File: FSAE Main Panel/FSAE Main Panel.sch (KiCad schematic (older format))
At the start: 11 parts, among them U1 SAMD21G18A-AU, Y101 32.768kHz

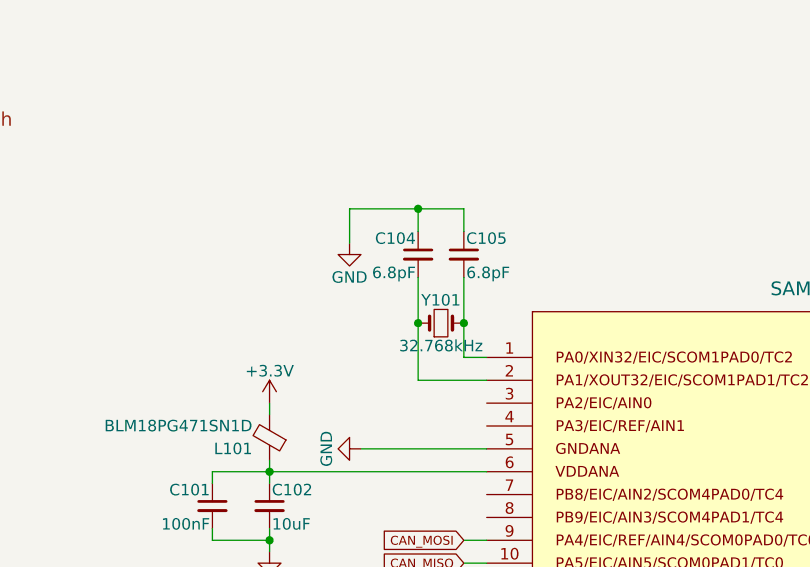
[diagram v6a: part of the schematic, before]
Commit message: Updated Footprint Association
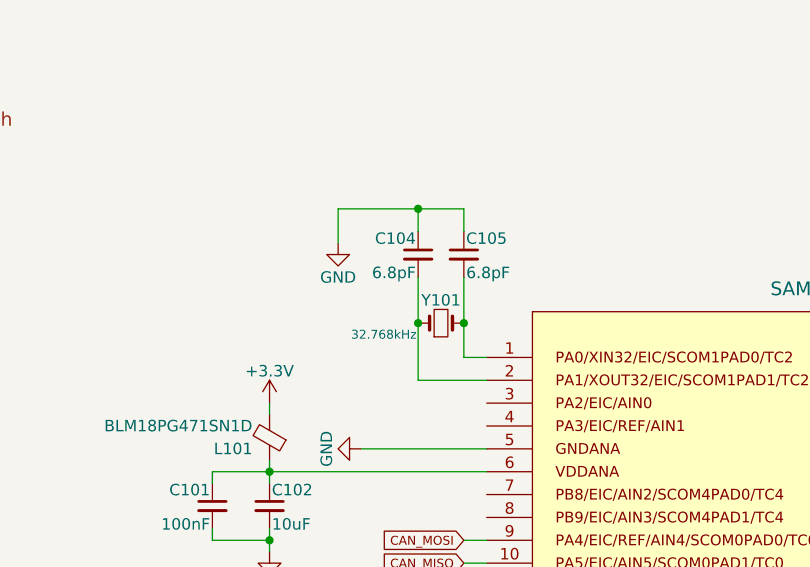
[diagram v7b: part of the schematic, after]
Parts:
- C101, C103, C106, C107: footprint (none) -> Capacitors_SMD:C_1206; Description (none) -> Ceramic 0.1uF 10V X7R 1206
- C102: footprint (none) -> Capacitors_SMD:C_1206; Description (none) -> Ceramic 10uF 25V X5R 1206
- C104, C105: footprint (none) -> Capacitors_SMD:C_0805; Description (none) -> Ceramic 6.8pF 50V C0G/NP0 0805
- C108: footprint (none) -> Capacitors_SMD:C_1206; Description (none) -> Ceramic 0.1uF 10V X7R
- L101: footprint (none) -> Inductors_SMD:L_1806
- U1: footprint (none) -> Housings_QFP:TQFP-48_7x7mm_Pitch0.5mm
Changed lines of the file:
@@
 F 0 "U1" H 5450 1800 60  0000 C CNN
 F 1 "SAMD21G18A-AU" H 5450 5000 60  0000 C CNN
-F 2 "" H 2350 3000 60  0001 C CNN
+F 2 "Housings_QFP:TQFP-48_7x7mm_Pitch0.5mm" H 2350 3000 60  0001 C CNN
 F 3 "" H 2350 3000 60  0001 C CNN
 	1    5450 3400
@@
 $EndComp
 $Comp
-L power:GND #PWR104
+L power:GND #PWR0104
 U 1 1 5BC6953B
-P 3250 1600
-F 0 "#PWR104" H 3250 1350 50  0001 C CNN
-F 1 "GND" H 3250 1450 50  0000 C CNN
-F 2 "" H 3250 1600 50  0001 C CNN
-F 3 "" H 3250 1600 50  0001 C CNN
-	1    3250 1600
-	1    0    0    -1
-$EndComp
-$Comp
-L power:+3V3 #PWR105
+P 3200 1600
+F 0 "#PWR0104" H 3200 1350 50  0001 C CNN
+F 1 "GND" H 3200 1450 50  0000 C CNN
+F 2 "" H 3200 1600 50  0001 C CNN
+F 3 "" H 3200 1600 50  0001 C CNN
+	1    3200 1600
+	1    0    0    -1
+$EndComp
+$Comp
+L power:+3V3 #PWR0105
 U 1 1 5BCFEE2B
 P 3250 3900
-F 0 "#PWR105" H 3250 3750 50  0001 C CNN
+F 0 "#PWR0105" H 3250 3750 50  0001 C CNN
 F 1 "+3V3" H 3250 4040 50  0000 C CNN
 F 2 "" H 3250 3900 50  0001 C CNN
@@
 $EndComp
 $Comp
-L power:+3V3 #PWR109
+L power:+3V3 #PWR0109
 U 1 1 5BCFEE84
 P 7150 3500
-F 0 "#PWR109" H 7150 3350 50  0001 C CNN
+F 0 "#PWR0109" H 7150 3350 50  0001 C CNN
 F 1 "+3V3" H 7150 3640 50  0000 C CNN
 F 2 "" H 7150 3500 50  0001 C CNN
@@
 $EndComp
 $Comp
-L power:+3V3 #PWR112
+L power:+3V3 #PWR0112
 U 1 1 5BCFEEDD
 P 7750 2400
-F 0 "#PWR112" H 7750 2250 50  0001 C CNN
+F 0 "#PWR0112" H 7750 2250 50  0001 C CNN
 F 1 "+3V3" H 7750 2540 50  0000 C CNN
 F 2 "" H 7750 2400 50  0001 C CNN
@@
 $EndComp
 $Comp
-L power:GND #PWR110
+L power:GND #PWR0110
 U 1 1 5BCFF22A
 P 7350 3700
-F 0 "#PWR110" H 7350 3450 50  0001 C CNN
+F 0 "#PWR0110" H 7350 3450 50  0001 C CNN
 F 1 "GND" H 7350 3550 50  0000 C CNN
 F 2 "" H 7350 3700 50  0001 C CNN
@@
 $EndComp
 $Comp
-L power:GND #PWR107
+L power:GND #PWR0107
 U 1 1 5BCFF970
 P 3300 4100
-F 0 "#PWR107" H 3300 3850 50  0001 C CNN
+F 0 "#PWR0107" H 3300 3850 50  0001 C CNN
 F 1 "GND" H 3300 3950 50  0000 C CNN
 F 2 "" H 3300 4100 50  0001 C CNN
@@
 $EndComp
 $Comp
-L power:GND #PWR108
+L power:GND #PWR0108
 U 1 1 5BCFFACD
 P 7150 2700
-F 0 "#PWR108" H 7150 2450 50  0001 C CNN
+F 0 "#PWR0108" H 7150 2450 50  0001 C CNN
 F 1 "GND" H 7150 2550 50  0000 C CNN
 F 2 "" H 7150 2700 50  0001 C CNN
@@
 $EndComp
 $Comp
-L power:GND #PWR101
+L power:GND #PWR0101
 U 1 1 5BD00189
 P 2800 4000
-F 0 "#PWR101" H 2800 3750 50  0001 C CNN
+F 0 "#PWR0101" H 2800 3750 50  0001 C CNN
 F 1 "GND" H 2800 3850 50  0000 C CNN
 F 2 "" H 2800 4000 50  0001 C CNN
@@
 $EndComp
 $Comp
-L power:GND #PWR113
+L power:GND #PWR0113
 U 1 1 5BD001EE
 P 8400 2600
-F 0 "#PWR113" H 8400 2350 50  0001 C CNN
+F 0 "#PWR0113" H 8400 2350 50  0001 C CNN
 F 1 "GND" H 8400 2450 50  0000 C CNN
 F 2 "" H 8400 2600 50  0001 C CNN
@@
 $EndComp
 $Comp
-L power:GND #PWR111
+L power:GND #PWR0111
 U 1 1 5BD006AA
 P 7550 3600
-F 0 "#PWR111" H 7550 3350 50  0001 C CNN
+F 0 "#PWR0111" H 7550 3350 50  0001 C CNN
 F 1 "GND" H 7550 3450 50  0000 C CNN
 F 2 "" H 7550 3600 50  0001 C CNN
@@
 Pins that support I2C: PA8, PA9, PA12, PA13, PA16, PA17, PA22, PA23
 $Comp
-L power:+3.3V #PWR102
+L power:+3.3V #PWR0102
 U 1 1 5BF9A879
 P 2900 2300
-F 0 "#PWR102" H 2900 2150 50  0001 C CNN
+F 0 "#PWR0102" H 2900 2150 50  0001 C CNN
 F 1 "+3.3V" H 2900 2440 50  0000 C CNN
 F 2 "" H 2900 2300 50  0001 C CNN
@@
 $EndComp
 $Comp
-L power:GND #PWR106
+L power:GND #PWR0106
 U 1 1 5BF9A928
 P 3300 2500
-F 0 "#PWR106" H 3300 2250 50  0001 C CNN
+F 0 "#PWR0106" H 3300 2250 50  0001 C CNN
 F 1 "GND" H 3300 2350 50  0000 C CNN
 F 2 "" H 3300 2500 50  0001 C CNN
@@
 $EndComp
 $Comp
-L power:GND #PWR103
+L power:GND #PWR0103
 U 1 1 5BF9AD79
 P 2900 2950
-F 0 "#PWR103" H 2900 2700 50  0001 C CNN
+F 0 "#PWR0103" H 2900 2700 50  0001 C CNN
 F 1 "GND" H 2900 2800 50  0000 C CNN
 F 2 "" H 2900 2950 50  0001 C CNN
@@
 F 0 "L101" H 2975 2500 50  0000 L CNN
 F 1 "BLM18PG471SN1D" H 2975 2400 50  0000 L CNN
-F 2 "" V 2830 2450 50  0001 C CNN
+F 2 "Inductors_SMD:L_1806" V 2830 2450 50  0001 C CNN
 F 3 "" H 2900 2450 50  0001 C CNN
 	1    2900 2450
@@
 F 0 "C102" H 2910 2820 50  0000 L CNN
 F 1 "10uF" H 2910 2670 50  0000 L CNN
-F 2 "" H 2900 2750 50  0001 C CNN
+F 2 "Capacitors_SMD:C_1206" H 2900 2750 50  0001 C CNN
 F 3 "" H 2900 2750 50  0001 C CNN
+F 4 "Ceramic 10uF 25V X5R 1206" H 2900 2750 50  0001 C CNN "Description"
 	1    2900 2750
 	1    0    0    -1
@@
 F 0 "C101" H 2660 2820 50  0000 L CNN
 F 1 "100nF" H 2660 2670 50  0000 L CNN
-F 2 "" H 2650 2750 50  0001 C CNN
+F 2 "Capacitors_SMD:C_1206" H 2650 2750 50  0001 C CNN
 F 3 "" H 2650 2750 50  0001 C CNN
+F 4 "Ceramic 0.1uF 10V X7R 1206" H 2650 2750 50  0001 C CNN "Description"
 	1    2650 2750
 	-1   0    0    -1
@@
 P 3650 1950
 F 0 "Y101" H 3650 2050 50  0000 C CNN
-F 1 "32.768kHz" H 3650 1850 50  0000 C CNN
+F 1 "32.768kHz" H 3400 1900 39  0000 C CNN
 F 2 "" H 3650 1950 50  0001 C CNN
 F 3 "" H 3650 1950 50  0001 C CNN
@@
 F 0 "C105" H 3760 1720 50  0000 L CNN
 F 1 "6.8pF" H 3760 1570 50  0000 L CNN
-F 2 "" H 3750 1650 50  0001 C CNN
+F 2 "Capacitors_SMD:C_0805" H 3750 1650 50  0001 C CNN
 F 3 "" H 3750 1650 50  0001 C CNN
+F 4 "Ceramic 6.8pF 50V C0G/NP0 0805" H 3750 1650 50  0001 C CNN "Description"
 	1    3750 1650
 	1    0    0    -1
@@
 F 0 "C104" H 3560 1720 50  0000 L CNN
 F 1 "6.8pF" H 3560 1570 50  0000 L CNN
-F 2 "" H 3550 1650 50  0001 C CNN
+F 2 "Capacitors_SMD:C_0805" H 3550 1650 50  0001 C CNN
 F 3 "" H 3550 1650 50  0001 C CNN
+F 4 "Ceramic 6.8pF 50V C0G/NP0 0805" H 3550 1650 50  0001 C CNN "Description"
 	1    3550 1650
 	-1   0    0    -1
@@
 F 0 "C103" H 3010 4070 50  0000 L CNN
 F 1 "100nF" H 3010 3920 50  0000 L CNN
-F 2 "" H 3000 4000 50  0001 C CNN
+F 2 "Capacitors_SMD:C_1206" H 3000 4000 50  0001 C CNN
 F 3 "" H 3000 4000 50  0001 C CNN
+F 4 "Ceramic 0.1uF 10V X7R 1206" H 3000 4000 50  0001 C CNN "Description"
 	1    3000 4000
 	0    -1   -1   0
@@
 F 0 "C106" H 7310 3670 50  0000 L CNN
 F 1 "100nF" H 7310 3520 50  0000 L CNN
-F 2 "" H 7300 3600 50  0001 C CNN
+F 2 "Capacitors_SMD:C_1206" H 7300 3600 50  0001 C CNN
 F 3 "" H 7300 3600 50  0001 C CNN
+F 4 "Ceramic 0.1uF 10V X7R 1206" H 7300 3600 50  0001 C CNN "Description"
 	1    7300 3600
 	0    -1   -1   0
@@
 F 0 "C107" H 7960 2570 50  0000 L CNN
 F 1 "100nF" H 7960 2420 50  0000 L CNN
-F 2 "" H 7950 2500 50  0001 C CNN
+F 2 "Capacitors_SMD:C_1206" H 7950 2500 50  0001 C CNN
 F 3 "" H 7950 2500 50  0001 C CNN
+F 4 "Ceramic 0.1uF 10V X7R 1206" H 7950 2500 50  0001 C CNN "Description"
 	1    7950 2500
 	0    -1   -1   0
@@
 F 0 "C108" H 8110 2670 50  0000 L CNN
 F 1 "100nF" H 8110 2520 50  0000 L CNN
-F 2 "" H 8100 2600 50  0001 C CNN
+F 2 "Capacitors_SMD:C_1206" H 8100 2600 50  0001 C CNN
 F 3 "" H 8100 2600 50  0001 C CNN
+F 4 "Ceramic 0.1uF 10V X7R" H 8100 2600 50  0001 C CNN "Description"
 	1    8100 2600
 	0    -1   1    0
@@
 	7550 4700 7650 4800
 Wire Wire Line
-	3250 1450 3550 1450
+	3200 1450 3550 1450
 Wire Wire Line
 	3550 1450 3750 1450
 Wire Wire Line
-	3250 1450 3250 1600
+	3200 1450 3200 1600
 Connection ~ 3550 1450
 Connection ~ 3750 1950

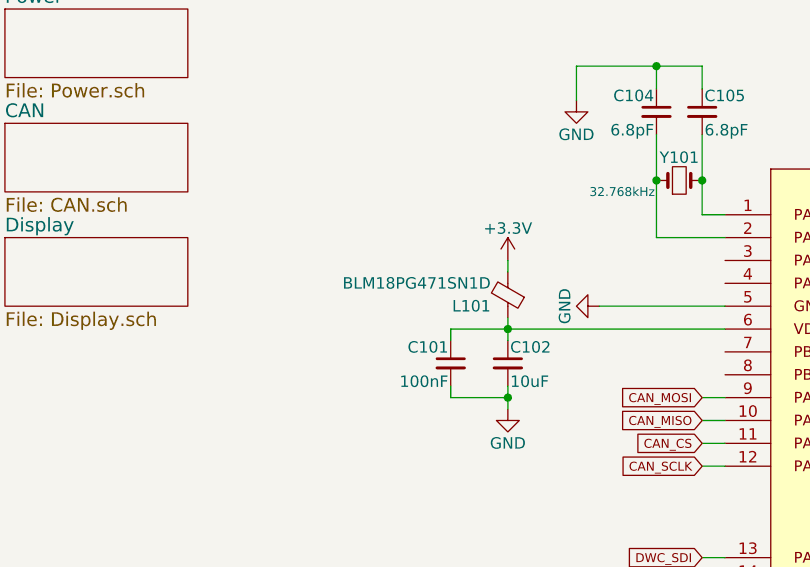
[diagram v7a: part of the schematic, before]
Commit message: New footprints, finished associating footprints
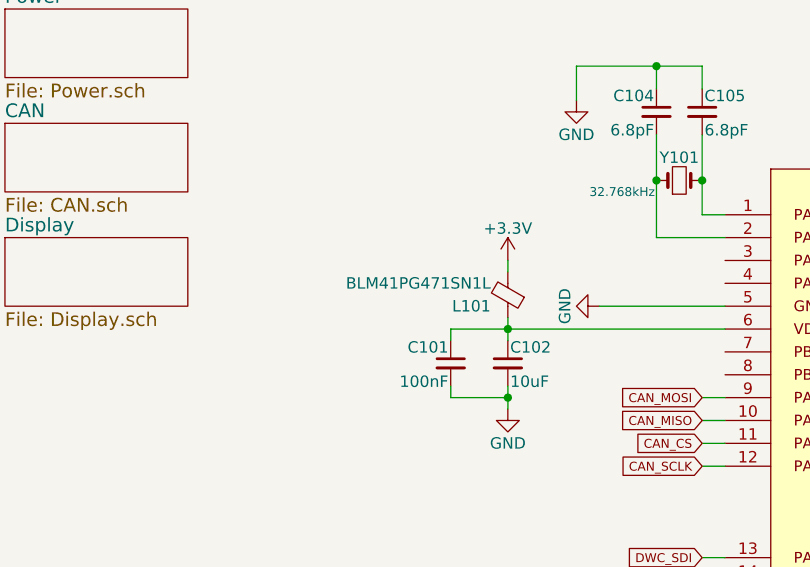
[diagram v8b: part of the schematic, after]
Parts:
- L101: value BLM18PG471SN1D -> BLM41PG471SN1L
- Y101: footprint (none) -> MS1V-T1K:MS1V-T1K
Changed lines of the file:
@@
 P 2900 2450
 F 0 "L101" H 2975 2500 50  0000 L CNN
-F 1 "BLM18PG471SN1D" H 2975 2400 50  0000 L CNN
+F 1 "BLM41PG471SN1L" H 2975 2400 50  0000 L CNN
 F 2 "Inductors_SMD:L_1806" V 2830 2450 50  0001 C CNN
 F 3 "" H 2900 2450 50  0001 C CNN
@@
 F 0 "Y101" H 3650 2050 50  0000 C CNN
 F 1 "32.768kHz" H 3400 1900 39  0000 C CNN
-F 2 "" H 3650 1950 50  0001 C CNN
+F 2 "MS1V-T1K:MS1V-T1K" H 3650 1950 50  0001 C CNN
 F 3 "" H 3650 1950 50  0001 C CNN
 	1    3650 1950
